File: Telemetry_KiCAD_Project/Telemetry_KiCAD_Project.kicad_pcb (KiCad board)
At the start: 2 copper layers, 62 parts, among them J1 50Ω SMA Connector, J2 DB37_Male, J3 10118192-0001LF, U2 Si4463, U3 ADL5521, U4 Si4463, U5 STM32L552CCU, U6 LM317T, U7 USBLC6-2SC6, Y1 30MHz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

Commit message: Initial PCB dimensions and production settings
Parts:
- added C29: 100nF, Capacitor_SMD:C_0603_1608Metric, F.Cu at (315.2, 50.3)
- added C30: 100nF, Capacitor_SMD:C_0603_1608Metric, F.Cu at (315.2, 52.8)
- added C31: 100nF, Capacitor_SMD:C_0603_1608Metric, F.Cu at (319.2, 50.3)
- added C32: 100nF, Capacitor_SMD:C_0603_1608Metric, F.Cu at (319.2, 52.8)
- added C33: 100nF, Capacitor_SMD:C_0603_1608Metric, F.Cu at (323.2, 50.3)
- C20: value 1uF -> 30pF
- C21: value 100nF -> 30pF
- C22: value 100nF -> 1uF
- C25, C26: value 30pF -> 100nF
- U5: value STM32L552CCU -> STM32L562VET; footprint Package_QFP:LQFP-48_7x7mm_P0.5mm -> Package_QFP:LQFP-100_14x14mm_P0.5mm
- moved U5 709.2 mm to (281.0, 131.6)
- moved C11 707.9 mm to (346.4, 96.8)
- moved C16 707.9 mm to (342.4, 96.8)
- moved C2 707.9 mm to (390.0, 57.8)
- moved C3 707.9 mm to (399.6, 47.7)
- moved C6 707.9 mm to (395.6, 50.3)
- moved C7 707.9 mm to (386.0, 57.8)
- moved C8 707.9 mm to (395.6, 47.7)
- moved C9 707.9 mm to (379.7, 85.2)
- moved J3 707.9 mm to (394.8, 67.2)
- moved L2 707.9 mm to (386.0, 52.8)
- moved L5 707.9 mm to (386.0, 55.3)
- moved L8 707.9 mm to (383.7, 85.2)
- moved R3 707.9 mm to (318.3, 99.0)
- moved R8 707.9 mm to (392.1, 71.4)
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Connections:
- C20 pad 1: +3V3 -> Net-(C20-Pad1)
- C21 pad 1: +3V3 -> Net-(C21-Pad1)
- C25 pad 1: Net-(C25-Pad1) -> +3V3
- C26 pad 1: Net-(C26-Pad1) -> +3V3
- J2 pad 12: /MCU_L552CC/ABORT_2 -> /MCU_L562VE/ABORT_2
- J2 pad 14: /MCU_L552CC/DEBUG_SWCLK -> /MCU_L562VE/DEBUG_SWCLK
- J2 pad 17: /MCU_L552CC/SPI1_MISO -> /MCU_L562VE/SPI1_MISO
- J2 pad 31: /MCU_L552CC/ABORT_1 -> /MCU_L562VE/ABORT_1
- J2 pad 33: /MCU_L552CC/DEBUG_SWDIO -> /MCU_L562VE/DEBUG_SWDIO
- J2 pad 35: /MCU_L552CC/SPI1_SCK -> /MCU_L562VE/SPI1_SCK
- J2 pad 36: /MCU_L552CC/SPI1_MOSI -> /MCU_L562VE/SPI1_MOSI
- U5 pad 10: Net-(U5-Pad10) -> GND
- U5 pad 11: /MCU_L552CC/SPI1_SCK -> +3V3
- U5 pad 12: Net-(U5-Pad12) -> Net-(C20-Pad1)
- U5 pad 13: /MCU_L552CC/ABORT_1 -> Net-(C21-Pad1)
- U5 pad 14: /~RX_SEL -> /37_Pin_DSUB_Bus/NRST
- U5 pad 15: /MCU_L552CC/ABORT_2 -> Net-(U5-Pad15)
- U5 pad 16: /MCU_L552CC/SPI1_MISO -> Net-(U5-Pad16)
- U5 pad 17: /MCU_L552CC/SPI1_MOSI -> Net-(U5-Pad17)
- U5 pad 18: /~TX_IRQ -> Net-(U5-Pad18)
- U5 pad 21: /TX_SCL -> +3V3
- U5 pad 23: GND -> Net-(U5-Pad23)
- U5 pad 24: +3V3 -> Net-(U5-Pad24)
- U5 pad 25: /~TX_SEL -> Net-(U5-Pad25)
- U5 pad 26: /~RX_IRQ -> GND
- U5 pad 27: /TX_SDO -> +3V3
- U5 pad 28: /TX_SDI -> /~RX_SEL
- U5 pad 29: Net-(U5-Pad29) -> /MCU_L562VE/SPI1_SCK
- U5 pad 30: Net-(U5-Pad30) -> /MCU_L562VE/SPI1_MISO
- U5 pad 31: Net-(U5-Pad31) -> /MCU_L562VE/SPI1_MOSI
- U5 pad 32: /USB Connector and ESD/D- -> /MCU_L562VE/~SPI1_NSS
- U5 pad 33: /USB Connector and ESD/D+ -> Net-(U5-Pad33)
- U5 pad 34: /MCU_L552CC/DEBUG_SWDIO -> Net-(U5-Pad34)
- U5 pad 35: GND -> Net-(U5-Pad35)
- U5 pad 36: +3V3 -> Net-(U5-Pad36)
- U5 pad 37: /MCU_L552CC/DEBUG_SWCLK -> Net-(U5-Pad37)
- U5 pad 39: /RX_SCL -> Net-(U5-Pad39)
- U5 pad 40: /RX_SDO -> Net-(U5-Pad40)
- U5 pad 41: /RX_SDI -> Net-(U5-Pad41)
- U5 pad 42: /37_Pin_DSUB_Bus/Alert_scl -> Net-(U5-Pad42)
- U5 pad 43: /37_Pin_DSUB_Bus/Alert_Active -> Net-(U5-Pad43)
- U5 pad 44: GND -> Net-(U5-Pad44)
- U5 pad 46: /37_Pin_DSUB_Bus/Alert_sda -> +3V3
- U5 pad 47: GND -> Net-(U5-Pad47)
- U5 pad 48: +3V3 -> Net-(U5-Pad48)
- U5 pad 5: Net-(C25-Pad1) -> Net-(U5-Pad5)
- U5 pad 6: Net-(C26-Pad1) -> +3V3
- U5 pad 7: /37_Pin_DSUB_Bus/NRST -> Net-(U5-Pad7)
- U5 pad 8: GND -> Net-(U5-Pad8)
- U5 pad 9: +3V3 -> Net-(U5-Pad9)
- Y3 pad 1: Net-(C25-Pad1) -> Net-(C20-Pad1)
- Y3 pad 2: Net-(C26-Pad1) -> Net-(C21-Pad1)
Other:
- board outline added: 80 x 87.3 mm
- copper layers 2 -> 4
- net class 900MHZ_RF_50OHM added: clearance 0.2, trace_width 0.25, via_dia 0.8, via_drill 0.4
- net class DIFF_90_USB added: clearance 1.25, trace_width 0.25, via_dia 0.8, via_drill 0.4
- rule trace_min: 0.2 -> 0.09
- rule via_min_drill: 0.3 -> 0.2

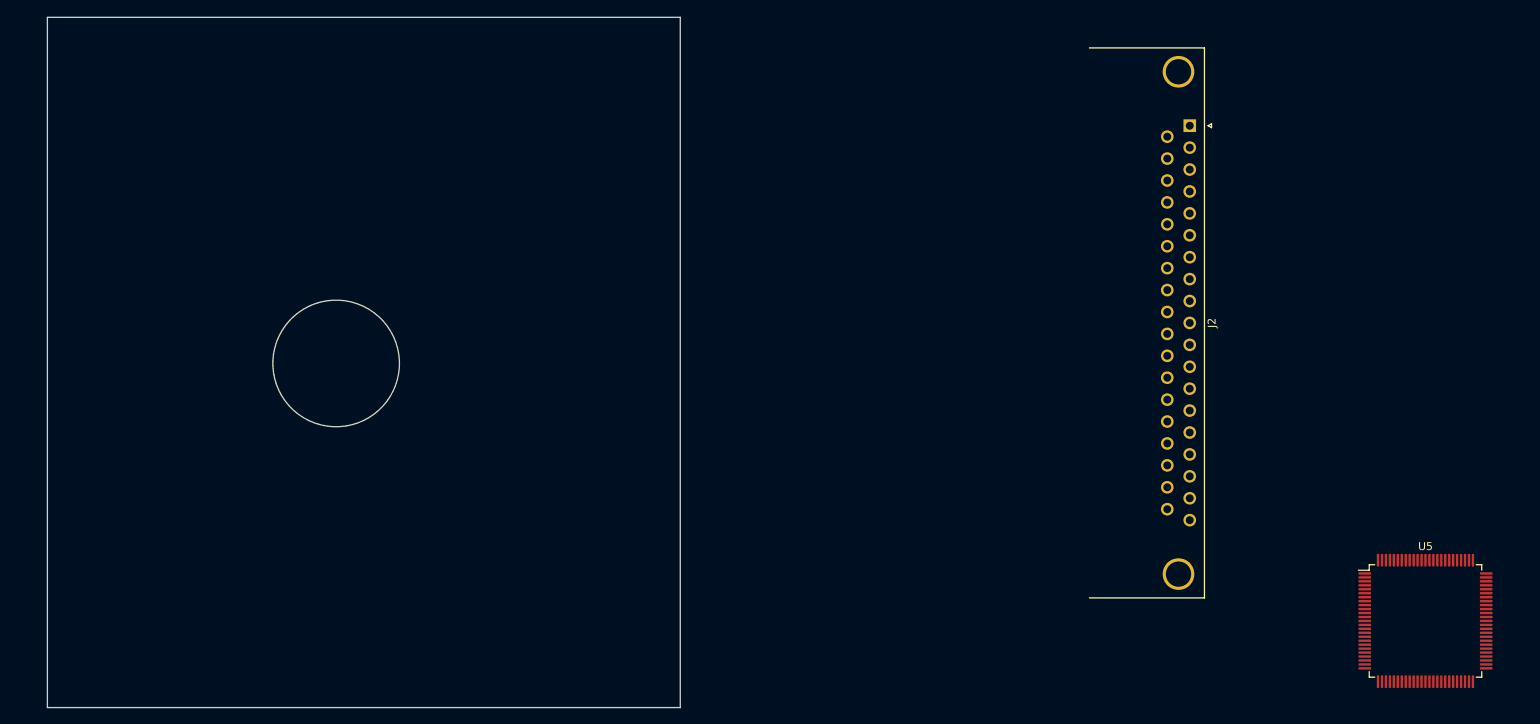
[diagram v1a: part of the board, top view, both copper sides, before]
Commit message: Placed DB37 connector
Might require some alignment later
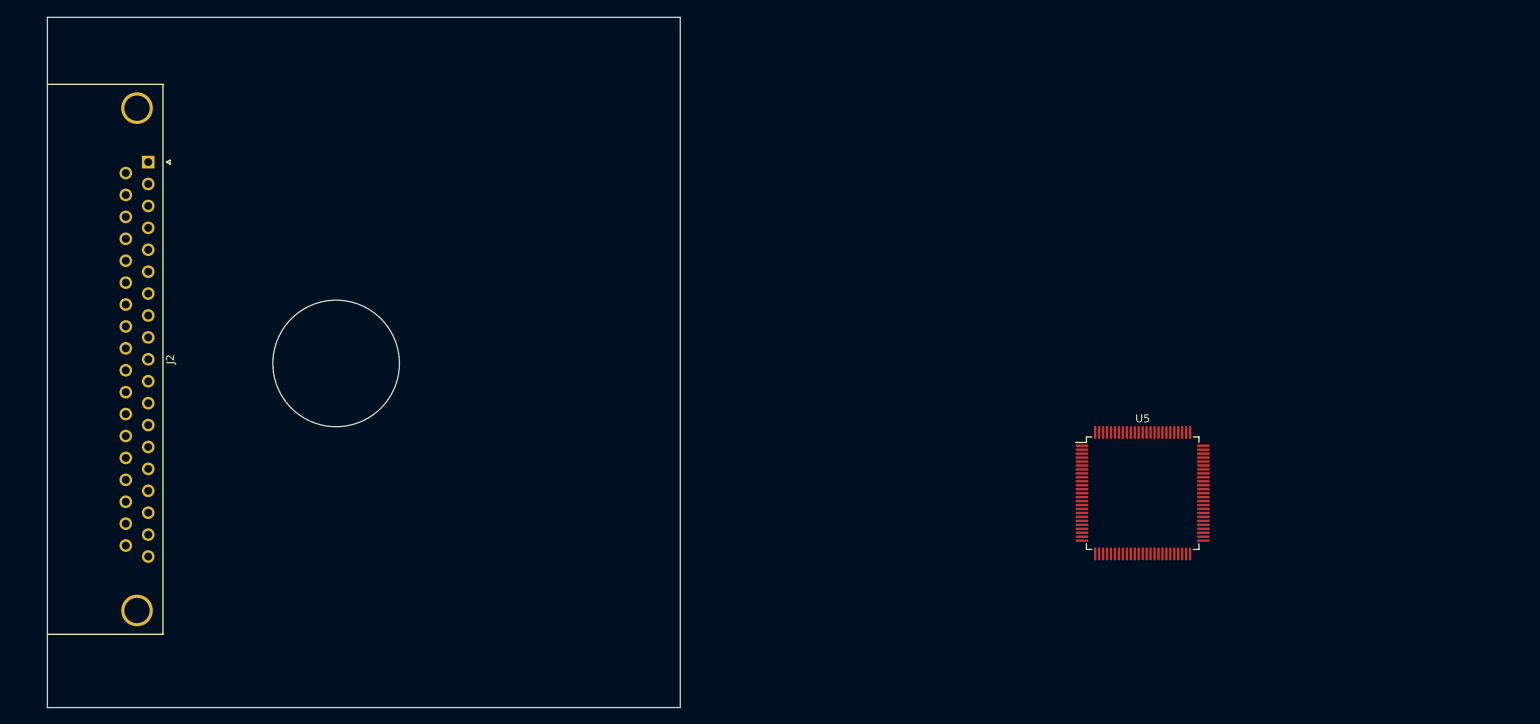
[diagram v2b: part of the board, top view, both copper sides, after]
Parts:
- moved J2 131.7 mm to (119.5, 73.6)
- moved U5 39.2 mm to (245.2, 115.5)
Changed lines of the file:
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@@
   (general
     (thickness 1.6)
-    (drawings 15)
+    (drawings 17)
     (tracks 0)
     (zones 0)
@@
   )
   (module Package_QFP:LQFP-100_14x14mm_P0.5mm (layer F.Cu)
-    (at 281 131.6)
+    (at 245.25 115.45)
     (descr "LQFP, 100 Pin (https://www.nxp.com/docs/en/package-information/SOT407-1.pdf), generated with kicad-footprint-generator ipc_gullwing_generator.py")
     (tags "LQFP QFP")
@@
   )
   (module Connector_Dsub:DSUB-37_Male_Horizontal_P2.77x2.84mm_EdgePinOffset9.90mm_Housed_MountingHolesOffset11.32mm (layer F.Cu)
-    (at 251.2 69 270)
+    (at 119.55 73.6 270)
     (descr "37-pin D-Sub connector, horizontal/angled (90 deg), THT-mount, male, pitch 2.77x2.84mm, pin-PCB-offset 9.9mm, distance of mounting holes 63.5mm, distance of mounting holes to PCB edge 11.32mm, see https://disti-assets.s3.amazonaws.com/tonar/files/datasheets/16730.pdf")
     (tags "37-pin D-Sub connector horizontal angled 90deg THT male pitch 2.77x2.84mm pin-PCB-offset 9.9mm mounting-holes-distance 63.5mm mounting-hole-offset 63.5mm")
@@
     )
   )
+  (dimension 8.8 (width 0.15) (layer Dwgs.User)
+    (gr_text "8.800 mm" (at 111.6 138.15 90) (layer Dwgs.User)
+      (effects (font (size 1 1) (thickness 0.15)))
+    )
+    (feature1 (pts (xy 106.8 133.75) (xy 110.886421 133.75)))
+    (feature2 (pts (xy 106.8 142.55) (xy 110.886421 142.55)))
+    (crossbar (pts (xy 110.3 142.55) (xy 110.3 133.75)))
+    (arrow1a (pts (xy 110.3 133.75) (xy 110.886421 134.876504)))
+    (arrow1b (pts (xy 110.3 133.75) (xy 109.713579 134.876504)))
+    (arrow2a (pts (xy 110.3 142.55) (xy 110.886421 141.423496)))
+    (arrow2b (pts (xy 110.3 142.55) (xy 109.713579 141.423496)))
+  )
+  (dimension 8 (width 0.15) (layer Dwgs.User)
+    (gr_text "8.000 mm" (at 99.65 59.3 270) (layer Dwgs.User)
+      (effects (font (size 1 1) (thickness 0.15)))
+    )
+    (feature1 (pts (xy 106.8 63.3) (xy 100.363579 63.3)))
+    (feature2 (pts (xy 106.8 55.3) (xy 100.363579 55.3)))
+    (crossbar (pts (xy 100.95 55.3) (xy 100.95 63.3)))
+    (arrow1a (pts (xy 100.95 63.3) (xy 100.363579 62.173496)))
+    (arrow1b (pts (xy 100.95 63.3) (xy 101.536421 62.173496)))
+    (arrow2a (pts (xy 100.95 55.3) (xy 100.363579 56.426504)))
+    (arrow2b (pts (xy 100.95 55.3) (xy 101.536421 56.426504)))
+  )
   (gr_circle (center 143.3 99.05) (end 151.3 99.05) (layer Edge.Cuts) (width 0.05))

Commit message: PCB Layout Progress
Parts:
- J3: footprint digikey-footprints:USB_Micro_B_Female_10118192 -> Connector_USB:USB_Micro-B_Amphenol_10118194_Horizontal
- U6: footprint digikey-footprints:TO-220-3 -> Package_TO_SOT_SMD:TO-252-3_TabPin2
- moved J3 239.2 mm to (165.0, 133.8), turned to 90 degrees
- moved C3 236.1 mm to (167.0, 88.4), turned to 270 degrees
- moved U7 230.6 mm to (158.2, 134.0)
- moved C2 225.5 mm to (167.0, 91.4), turned to 90 degrees
- moved C10 224.9 mm to (161.5, 108.4)
- moved L8 224.9 mm to (160.5, 113.0)
- moved R1 224.9 mm to (163.2, 110.6)
- moved L7 224.9 mm to (165.5, 108.4)
- moved R2 224.9 mm to (160.8, 110.6)
- moved C1 222.9 mm to (168.4, 88.4), turned to 270 degrees
- moved U2 221.8 mm to (161.8, 89.4), turned to 90 degrees
- moved R8 217.6 mm to (179.7, 118.8)
- moved R7 217.6 mm to (177.2, 118.8)
- moved U3 207.5 mm to (173.8, 102.8)
- moved C9 197.1 mm to (183.6, 105.0), turned to 90 degrees
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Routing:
- net /~RX_SEL: track 0.00 -> 29.1 mm, vias 0 -> 2
- net /~RX_IRQ: track 0.00 -> 21.7 mm, vias 0 -> 2
- net /~TX_SEL: track 0.00 -> 19.9 mm, vias 0 -> 2
- net /TX_SCL: track 0.00 -> 18.5 mm, vias 0 -> 2
- net /TX_SDO: track 0.00 -> 17.0 mm, vias 0 -> 2
- net /TX_SDI: track 0.00 -> 15.3 mm, vias 0 -> 2
- net /~TX_IRQ: track 0.00 -> 12.2 mm
- net /RX_SCL: track 0.00 -> 11.3 mm, vias 0 -> 2
- net /RX_SDO: track 0.00 -> 10.8 mm, vias 0 -> 2
- net /RX_SDI: track 0.00 -> 10.7 mm, vias 0 -> 2
- net +3V3: track 0.00 -> 10.2 mm, vias 0 -> 1
- net GND: track 0.00 -> 8.38 mm, vias 0 -> 3
- added copper zone on Pwr.Cu, net +3V3
- added copper zone on Gnd.Cu, net GND

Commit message: PCB Layout Progress
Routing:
- net +3V3: track 10.2 -> 21.4 mm
- net GND: track 8.38 -> 12.8 mm, vias 3 -> 5
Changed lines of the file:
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@@
     (thickness 1.6)
     (drawings 17)
-    (tracks 114)
+    (tracks 133)
     (zones 0)
     (modules 67)
@@
   (segment (start 182.4 89.4) (end 183 89.4) (width 0.25) (layer Gnd.Cu) (net 1))
   (segment (start 182.5875 89.4) (end 182.8 89.1875) (width 0.25) (layer F.Cu) (net 1))
-  (segment (start 180.525 89.4) (end 182.5875 89.4) (width 0.25) (layer F.Cu) (net 1))
   (segment (start 182.8 90.6125) (end 182.8 89.1875) (width 0.25) (layer F.Cu) (net 1))
   (segment (start 184.4 89.1875) (end 182.8 89.1875) (width 0.25) (layer F.Cu) (net 1))
@@
   (segment (start 184.3875 90.6125) (end 184.4 90.6) (width 0.25) (layer F.Cu) (net 1))
   (segment (start 182.8 90.6125) (end 184.3875 90.6125) (width 0.25) (layer F.Cu) (net 1))
+  (segment (start 166.7875 89.4) (end 167 89.1875) (width 0.25) (layer F.Cu) (net 1))
+  (segment (start 167 89.1875) (end 168.4 89.1875) (width 0.25) (layer F.Cu) (net 1))
+  (segment (start 167 90.6125) (end 167 89.1875) (width 0.25) (layer F.Cu) (net 1))
+  (segment (start 180.525 89.4) (end 181.4 89.4) (width 0.25) (layer F.Cu) (net 1))
+  (segment (start 165.2 90.4) (end 166.2 89.4) (width 0.25) (layer F.Cu) (net 1))
+  (segment (start 163.725 90.4) (end 165.2 90.4) (width 0.25) (layer F.Cu) (net 1))
+  (segment (start 166.2 89.4) (end 166.7875 89.4) (width 0.25) (layer F.Cu) (net 1))
+  (segment (start 163.725 89.4) (end 166.2 89.4) (width 0.25) (layer F.Cu) (net 1))
+  (segment (start 181.2 90.4) (end 182.2 89.4) (width 0.25) (layer F.Cu) (net 1))
+  (segment (start 180.525 90.4) (end 181.2 90.4) (width 0.25) (layer F.Cu) (net 1))
+  (segment (start 182.2 89.4) (end 182.5875 89.4) (width 0.25) (layer F.Cu) (net 1))
+  (segment (start 181.4 89.4) (end 182.2 89.4) (width 0.25) (layer F.Cu) (net 1))
   (via (at 121.4 123.4) (size 0.8) (drill 0.4) (layers F.Cu B.Cu) (net 2))
   (segment (start 121.34 123.46) (end 121.4 123.4) (width 0.25) (layer F.Cu) (net 2))
@@
   (segment (start 182.8 92.1875) (end 183.9875 92.1875) (width 0.25) (layer F.Cu) (net 2))
   (segment (start 184 92.2) (end 184.2 92) (width 0.25) (layer Gnd.Cu) (net 2))
+  (via (at 167.8 86.4) (size 0.8) (drill 0.4) (layers F.Cu B.Cu) (net 2))
+  (segment (start 167 87.2) (end 167.8 86.4) (width 0.25) (layer F.Cu) (net 2))
+  (segment (start 167 87.6125) (end 167 87.2) (width 0.25) (layer F.Cu) (net 2))
+  (segment (start 167.8 87.0125) (end 168.4 87.6125) (width 0.25) (layer F.Cu) (net 2))
+  (segment (start 167.8 86.4) (end 167.8 87.0125) (width 0.25) (layer F.Cu) (net 2))
+  (via (at 168.4 92.2) (size 0.8) (drill 0.4) (layers F.Cu B.Cu) (net 2))
+  (segment (start 168.3875 92.1875) (end 168.4 92.2) (width 0.25) (layer F.Cu) (net 2))
+  (segment (start 167 92.1875) (end 168.3875 92.1875) (width 0.25) (layer F.Cu) (net 2))
   (segment (start 162.8 87.475) (end 163.4 86.875) (width 0.25) (layer F.Cu) (net 58))
   (segment (start 163.4 79.2) (end 165.972955 76.627045) (width 0.25) (layer F.Cu) (net 58))
